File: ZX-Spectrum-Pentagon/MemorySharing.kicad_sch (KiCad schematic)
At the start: 9 parts, among them U11 74HC02, U31 74HC32, U32 74HC00, U33 74HC74, U34 74HC08, U4 74HC11, U7 74HC04, U8 74HC00, U9 74HC86

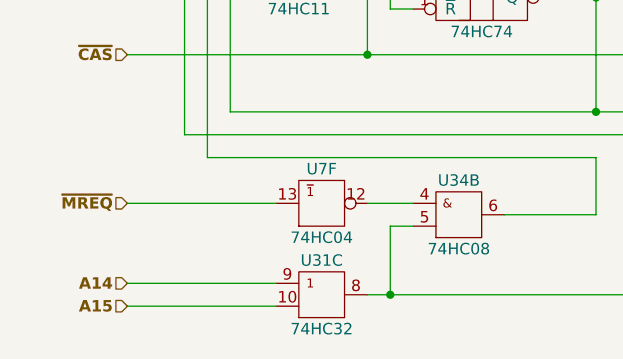
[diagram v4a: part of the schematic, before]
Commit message: reconnect U31 trace U31 tracing
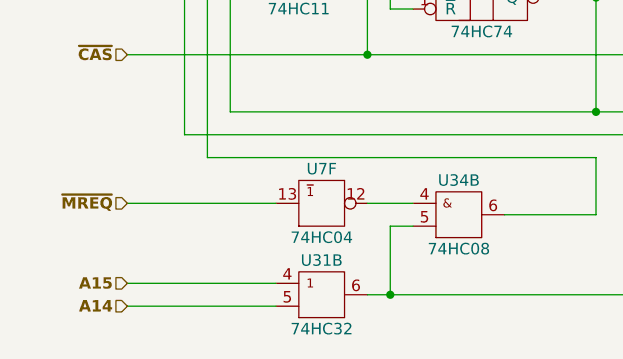
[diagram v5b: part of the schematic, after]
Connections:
- net A14: now also U31.5 (B); no longer U31.9 (A)
- net A15: now also U31.4 (A); no longer U31.10 (B)
- net ~{FQUATER}: now also U31.6 (Y); no longer U31.8 (Y)
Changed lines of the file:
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@@
     (effects (font (size 1.27 1.27) (thickness 0.254) bold) (justify right))
   )
-  (hierarchical_label "A14" (shape input) (at 31.75 111.76 180)
+  (hierarchical_label "A14" (shape input) (at 31.75 114.3 180)
     (effects (font (size 1.27 1.27) (thickness 0.254) bold) (justify right))
   )
@@
     (effects (font (size 1.27 1.27) (thickness 0.254) bold) (justify left))
   )
-  (hierarchical_label "A15" (shape input) (at 31.75 114.3 180)
+  (hierarchical_label "A15" (shape input) (at 31.75 111.76 180)
     (effects (font (size 1.27 1.27) (thickness 0.254) bold) (justify right))
   )
@@
     (pin "9")
   )
-  (symbol (lib_id "74IEC:74HC32") (at 53.34 113.03 0) (unit 3)
+  (symbol (lib_id "74IEC:74HC32") (at 53.34 113.03 0) (unit 2)
     (in_bom yes) (on_board yes)
     (property "Reference" "U31" (id 0) (at 53.34 109.22 0))

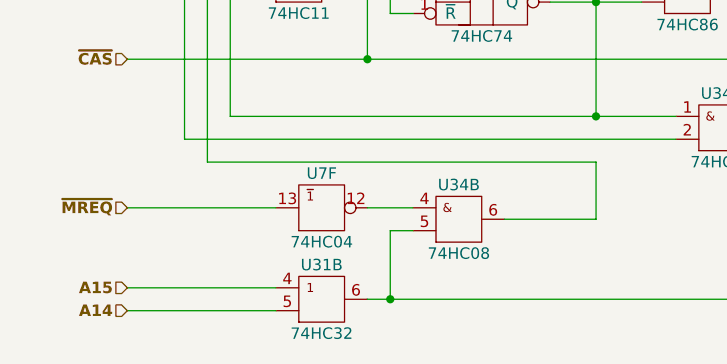
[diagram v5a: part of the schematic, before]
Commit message: reconection U31 rotate LVE1
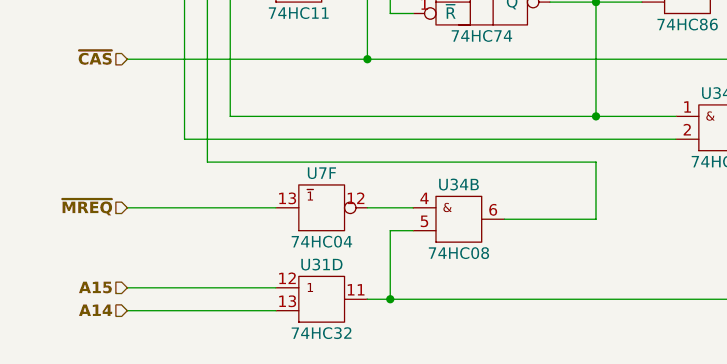
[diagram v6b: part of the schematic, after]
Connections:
- net A14: now also U31.13 (B); no longer U31.5 (B)
- net A15: now also U31.12 (A); no longer U31.4 (A)
- net ~{FQUATER}: now also U31.11 (Y); no longer U31.6 (Y)
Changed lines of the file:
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@@
     (pin "9")
   )
-  (symbol (lib_id "74IEC:74HC32") (at 53.34 113.03 0) (unit 2)
+  (symbol (lib_id "74IEC:74HC32") (at 53.34 113.03 0) (unit 4)
     (in_bom yes) (on_board yes)
     (property "Reference" "U31" (id 0) (at 53.34 109.22 0))

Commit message: tracing
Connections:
- net DISPLAY: now also U34.12 (A); no longer U34.1 (A)
- net RAS: now also U34.13 (B); no longer U34.2 (B)
- net ~{FQUATER}: now also U34.10 (B); no longer U34.5 (B)
- net at U7.12 (~{Y}): now also U34.9 (A); no longer U34.4 (A)
- net at U32.2 (B), U4.10 (B), U8.13 (B): now also U34.8 (~{Y}); no longer U34.6 (~{Y})
- net at U32.10 (B), U32.13 (B): now also U34.11 (~{Y}); no longer U34.3 (~{Y})
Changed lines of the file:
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@@
     (pin "13")
   )
-  (symbol (lib_id "74IEC:74HC08") (at 68.58 104.14 0) (unit 2)
+  (symbol (lib_id "74IEC:74HC08") (at 68.58 104.14 0) (unit 3)
     (in_bom yes) (on_board yes)
     (property "Reference" "U34" (id 0) (at 68.58 100.33 0))
@@
     (pin "13")
   )
-  (symbol (lib_id "74IEC:74HC08") (at 97.79 93.98 0) (unit 1)
+  (symbol (lib_id "74IEC:74HC08") (at 97.79 93.98 0) (unit 4)
     (in_bom yes) (on_board yes)
     (property "Reference" "U34" (id 0) (at 97.79 90.17 0))

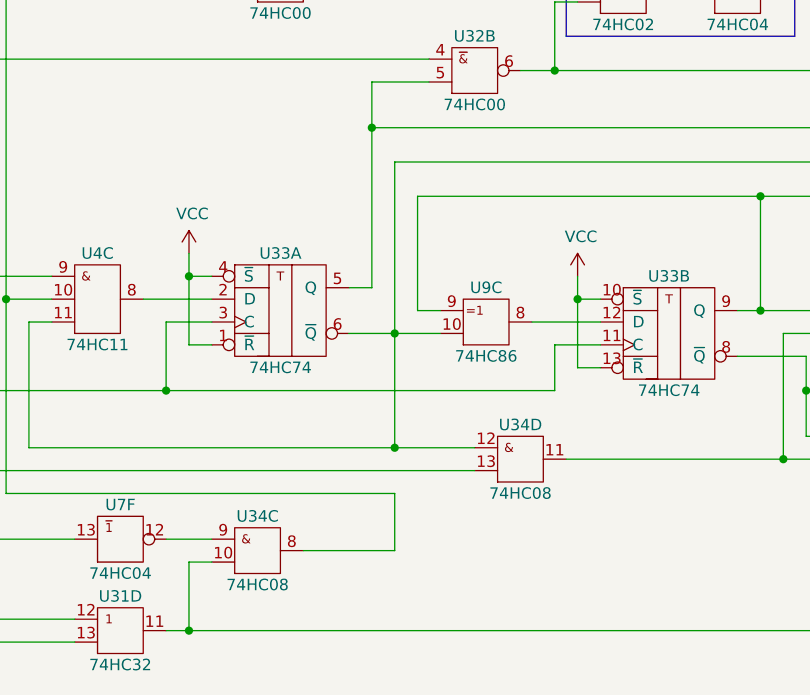
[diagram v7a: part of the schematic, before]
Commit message: tracing generator
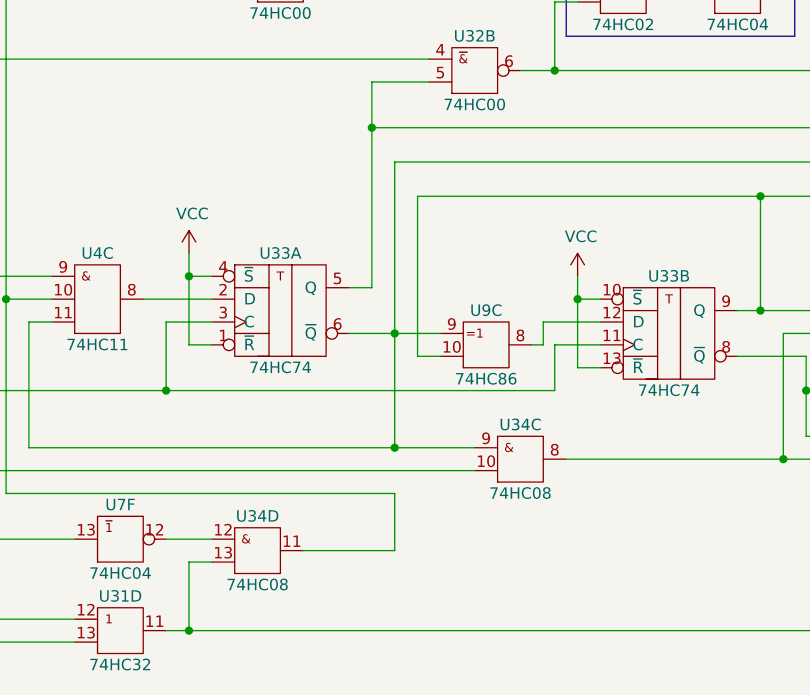
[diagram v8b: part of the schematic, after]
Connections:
- net C29: now also U9.10 (B); no longer U9.9 (A)
- net DISPLAY: now also U34.9 (A), U9.9 (A); no longer U34.12 (A), U9.10 (B)
- net RAS: now also U34.10 (B); no longer U34.13 (B)
- net ~{FQUATER}: now also U34.13 (B); no longer U34.10 (B)
- net at U7.12 (~{Y}): now also U34.12 (A); no longer U34.9 (A)
- net at U32.2 (B), U4.10 (B), U8.13 (B): now also U34.11 (~{Y}); no longer U34.8 (~{Y})
- net at U32.10 (B), U32.13 (B): now also U34.8 (~{Y}); no longer U34.11 (~{Y})
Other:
- moved on the sheet: U9C
